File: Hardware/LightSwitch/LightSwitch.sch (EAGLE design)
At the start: 19 parts, among them IC1 ATMEGA328P, Q1 8MHz, X1 MAINS

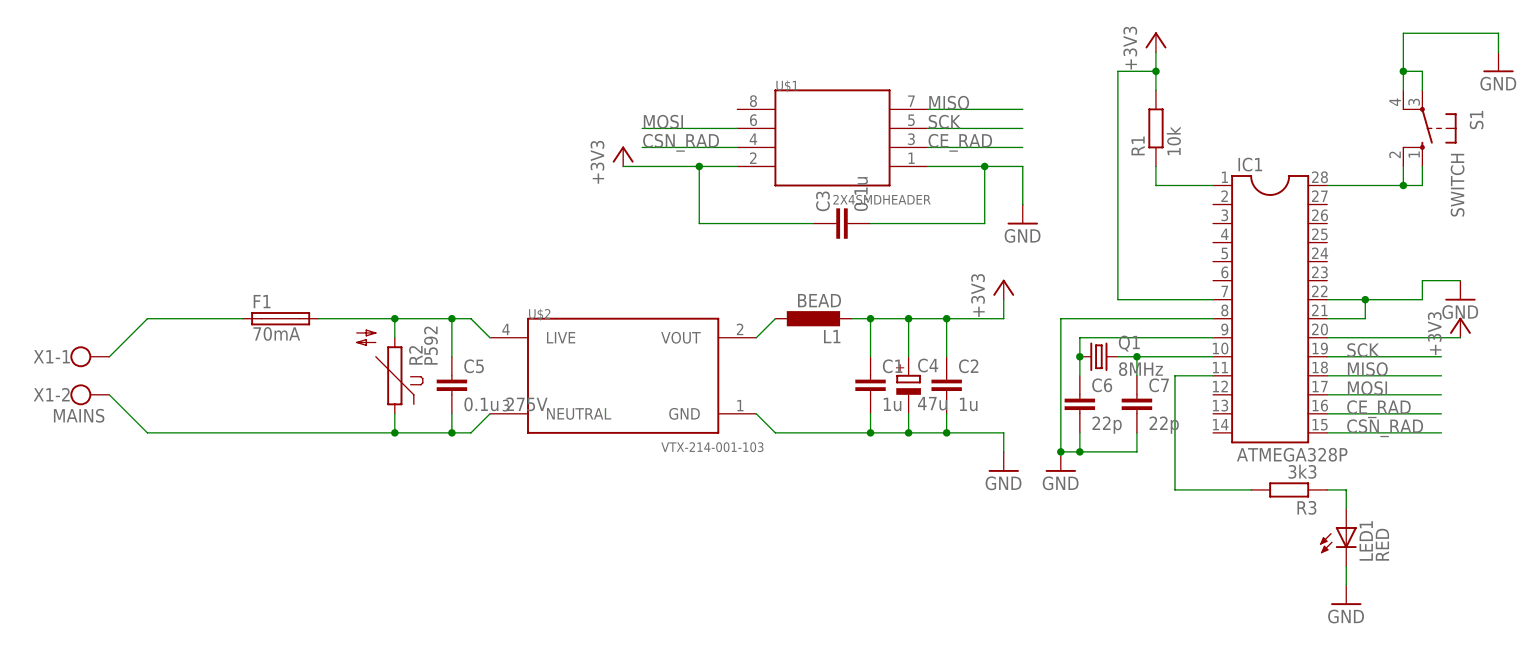
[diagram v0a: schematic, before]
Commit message: updated schematic and created intial wired design for light switch
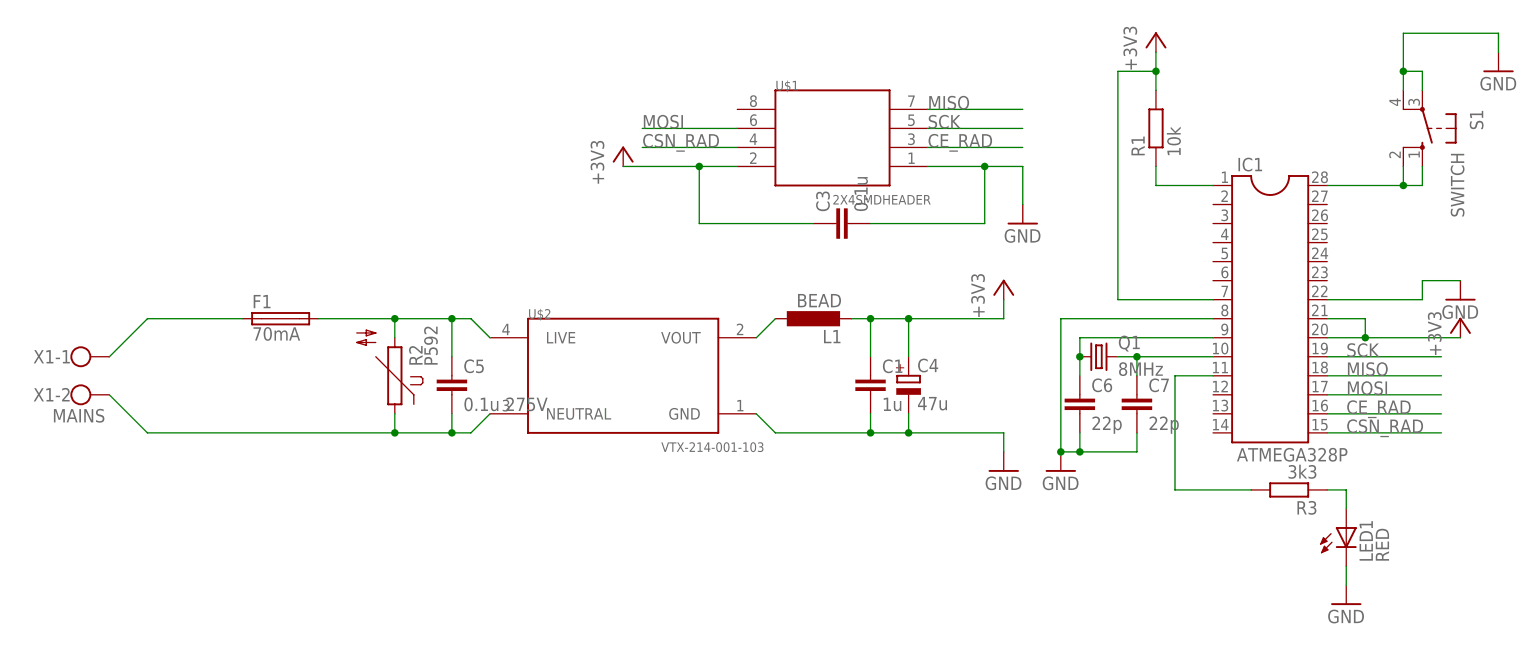
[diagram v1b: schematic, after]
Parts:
- removed C2: 1u, rcl:C-EUC1206
- C1: device rcl:C-EU025-025X050 -> rcl:C-EUC1206K
- F1: device fuse:SH25 -> fuse:FUSESH22,5A
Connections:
- net +3V3: now also IC1.21; no longer C2.1
- net GND: no longer C2.2, IC1.21
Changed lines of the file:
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@@
 <part name="S1" library="switch-omron" deviceset="40-XX" device="" value="SWITCH"/>
 <part name="R2" library="varistor" deviceset="P592" device=""/>
-<part name="F1" library="fuse" deviceset="SH25" device="" value="70mA"/>
+<part name="F1" library="fuse" deviceset="FUSE" device="SH22,5A" value="70mA"/>
 <part name="LED1" library="led" deviceset="LED" device="5MM" value="RED"/>
 <part name="R3" library="rcl" deviceset="R-EU_" device="R1206" value="3k3"/>
-<part name="C1" library="rcl" deviceset="C-EU" device="025-025X050" value="1u"/>
-<part name="C2" library="rcl" deviceset="C-EU" device="C1206" value="1u"/>
+<part name="C1" library="rcl" deviceset="C-EU" device="C1206K" value="1u"/>
 <part name="C3" library="rcl" deviceset="C-EU" device="C1206" value="0.1u"/>
 <part name="C4" library="rcl" deviceset="CPOL-EU" device="E2,5-6E" value="47u"/>
@@
 <instance part="S1" gate="1" x="121.92" y="68.58" rot="R180"/>
 <instance part="R2" gate="1" x="-15.24" y="35.56" rot="R90"/>
-<instance part="F1" gate="1" x="-30.48" y="43.18"/>
+<instance part="F1" gate="G$1" x="-30.48" y="43.18"/>
 <instance part="LED1" gate="G$1" x="111.76" y="15.24"/>
 <instance part="R3" gate="G$1" x="104.14" y="20.32" rot="R180"/>
 <instance part="C1" gate="G$1" x="48.26" y="35.56"/>
-<instance part="C2" gate="G$1" x="58.42" y="35.56"/>
 <instance part="C3" gate="G$1" x="43.18" y="55.88" rot="R90"/>
 <instance part="C4" gate="G$1" x="53.34" y="35.56"/>
@@
 <wire x1="48.26" y1="43.18" x2="48.26" y2="38.1" width="0.1524" layer="91"/>
 <pinref part="C4" gate="G$1" pin="+"/>
-<wire x1="58.42" y1="43.18" x2="53.34" y2="43.18" width="0.1524" layer="91"/>
 <wire x1="53.34" y1="43.18" x2="48.26" y2="43.18" width="0.1524" layer="91"/>
 <wire x1="53.34" y1="38.1" x2="53.34" y2="43.18" width="0.1524" layer="91"/>
 <junction x="53.34" y="43.18"/>
-<pinref part="C2" gate="G$1" pin="1"/>
-<wire x1="58.42" y1="38.1" x2="58.42" y2="43.18" width="0.1524" layer="91"/>
 <junction x="48.26" y="43.18"/>
-<junction x="58.42" y="43.18"/>
 <pinref part="L1" gate="G$1" pin="2"/>
 <wire x1="48.26" y1="43.18" x2="45.72" y2="43.18" width="0.1524" layer="91"/>
-<wire x1="58.42" y1="43.18" x2="66.04" y2="43.18" width="0.1524" layer="91"/>
+<wire x1="53.34" y1="43.18" x2="66.04" y2="43.18" width="0.1524" layer="91"/>
 </segment>
 <segment>
@@
 <pinref part="IC1" gate="G$1" pin="20"/>
 <pinref part="+3V4" gate="G$1" pin="+3V3"/>
-<wire x1="109.22" y1="40.64" x2="127" y2="40.64" width="0.1524" layer="91"/>
+<wire x1="109.22" y1="40.64" x2="114.3" y2="40.64" width="0.1524" layer="91"/>
+<pinref part="IC1" gate="G$1" pin="21"/>
+<wire x1="114.3" y1="40.64" x2="127" y2="40.64" width="0.1524" layer="91"/>
+<wire x1="109.22" y1="43.18" x2="114.3" y2="43.18" width="0.1524" layer="91"/>
+<wire x1="114.3" y1="43.18" x2="114.3" y2="40.64" width="0.1524" layer="91"/>
+<junction x="114.3" y="40.64"/>
 </segment>
 </net>
@@
 <junction x="48.26" y="27.94"/>
 <junction x="53.34" y="27.94"/>
-<pinref part="C2" gate="G$1" pin="2"/>
-<wire x1="58.42" y1="30.48" x2="58.42" y2="27.94" width="0.1524" layer="91"/>
-<wire x1="58.42" y1="27.94" x2="53.34" y2="27.94" width="0.1524" layer="91"/>
-<junction x="58.42" y="27.94"/>
 <pinref part="GND1" gate="1" pin="GND"/>
-<wire x1="58.42" y1="27.94" x2="66.04" y2="27.94" width="0.1524" layer="91"/>
+<wire x1="53.34" y1="27.94" x2="66.04" y2="27.94" width="0.1524" layer="91"/>
 <wire x1="66.04" y1="27.94" x2="66.04" y2="25.4" width="0.1524" layer="91"/>
 </segment>
@@
 <segment>
 <pinref part="IC1" gate="G$1" pin="22"/>
-<wire x1="109.22" y1="45.72" x2="114.3" y2="45.72" width="0.1524" layer="91"/>
-<wire x1="114.3" y1="45.72" x2="121.92" y2="45.72" width="0.1524" layer="91"/>
+<wire x1="109.22" y1="45.72" x2="121.92" y2="45.72" width="0.1524" layer="91"/>
 <wire x1="121.92" y1="45.72" x2="121.92" y2="48.26" width="0.1524" layer="91"/>
 <wire x1="121.92" y1="48.26" x2="127" y2="48.26" width="0.1524" layer="91"/>
 <pinref part="GND6" gate="1" pin="GND"/>
-<pinref part="IC1" gate="G$1" pin="21"/>
-<wire x1="109.22" y1="43.18" x2="114.3" y2="43.18" width="0.1524" layer="91"/>
-<wire x1="114.3" y1="43.18" x2="114.3" y2="45.72" width="0.1524" layer="91"/>
-<junction x="114.3" y="45.72"/>
 </segment>
 </net>
@@
 <wire x1="-2.54" y1="40.64" x2="-5.08" y2="43.18" width="0.1524" layer="91"/>
 <wire x1="-5.08" y1="43.18" x2="-7.62" y2="43.18" width="0.1524" layer="91"/>
-<pinref part="F1" gate="1" pin="2"/>
+<pinref part="F1" gate="G$1" pin="2"/>
 <pinref part="R2" gate="1" pin="2"/>
 <wire x1="-7.62" y1="43.18" x2="-15.24" y2="43.18" width="0.1524" layer="91"/>
@@
 <junction x="-7.62" y="27.94"/>
 <pinref part="X1" gate="-2" pin="KL"/>
-<wire x1="-48.26" y1="27.94" x2="-53.34" y2="33.02" width="0.1524" layer="91"/>
+<wire x1="-53.34" y1="33.02" x2="-48.26" y2="27.94" width="0.1524" layer="91"/>
 </segment>
 </net>
@@
 <net name="N$1" class="0">
 <segment>
-<pinref part="F1" gate="1" pin="1"/>
+<pinref part="F1" gate="G$1" pin="1"/>
 <wire x1="-35.56" y1="43.18" x2="-48.26" y2="43.18" width="0.1524" layer="91"/>
 <pinref part="X1" gate="-1" pin="KL"/>
-<wire x1="-48.26" y1="43.18" x2="-53.34" y2="38.1" width="0.1524" layer="91"/>
-</segment>
-</net>
+<wire x1="-53.34" y1="38.1" x2="-48.26" y2="43.18" width="0.1524" layer="91"/>
+</segment>
+</net>

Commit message: added mounting holes to include extra detail for silk
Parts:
- added H1, H2: MOUNT-HOLE4.1, holes:MOUNT-HOLE4.1
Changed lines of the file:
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@@
 <part name="C6" library="rcl" deviceset="C-EU" device="C1206" value="22p"/>
 <part name="C7" library="rcl" deviceset="C-EU" device="C1206" value="22p"/>
+<part name="H1" library="holes" deviceset="MOUNT-HOLE" device="4.1"/>
+<part name="H2" library="holes" deviceset="MOUNT-HOLE" device="4.1"/>
 </parts>
 <sheets>
@@
 <instance part="C6" gate="G$1" x="76.2" y="33.02"/>
 <instance part="C7" gate="G$1" x="83.82" y="33.02"/>
+<instance part="H1" gate="G$1" x="10.16" y="12.7"/>
+<instance part="H2" gate="G$1" x="38.1" y="12.7"/>
 </instances>
 <busses>
